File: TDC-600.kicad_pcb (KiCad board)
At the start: 2 copper layers, 99.9 x 64 mm, 32 parts, among them J1 MSXCART1, J2 Conn_01x03_Male, J3 Conn_01x03_Male, J4 Conn_01x03_Male, J5 Conn_01x03_Male, J6 FDD Connector, J7 ROM_SWITCH, SW1 SW_Push, U1 AT28C256, U2 74LS04, U3 74LS138, U4 WDC37C65, Y1 16Mhz

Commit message: Routing Release 1.0
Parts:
- J1: footprint Roni Footprints:MSX_CART_SW_Official_3Holes -> Roni_Footprints:MSX_CART_SW_Official
- moved R1 8.03 mm to (128.5, 48.5), turned to 180 degrees
- moved R11 2.84 mm to (122.7, 69.6)
- moved R9 0.48 mm to (82.4, 69.6)
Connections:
- J1 pad 41: Net-(J1-Pad41) -> GNDREF
- J1 pad 43: Net-(J1-Pad41) -> GNDREF
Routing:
- net GNDREF: track 0.00 -> 268.6 mm, vias 0 -> 5
- net +5V: track 0.00 -> 138.2 mm, vias 0 -> 1
- net /SLTSL: track 0.00 -> 125.7 mm, vias 0 -> 4
- net A14: track 0.00 -> 109.1 mm, vias 0 -> 4
- net /RESET: track 0.00 -> 106.1 mm, vias 0 -> 3
- net D7: track 0.00 -> 99.0 mm, vias 0 -> 2
- net A15: track 0.00 -> 96.6 mm, vias 0 -> 2
- net WDRST: track 0.00 -> 93.7 mm, vias 0 -> 2
- net A12: track 0.00 -> 92.0 mm, vias 0 -> 2
- net D6: track 0.00 -> 91.0 mm, vias 0 -> 1
- net /WR: track 0.00 -> 89.5 mm, vias 0 -> 3
- net A13: track 0.00 -> 87.0 mm
- net D5: track 0.00 -> 86.0 mm, vias 0 -> 2
- net A8: track 0.00 -> 81.8 mm, vias 0 -> 2
- net D4: track 0.00 -> 79.6 mm, vias 0 -> 1
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- added copper zone on B.Cu, net GNDREF
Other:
- outline, holes or cut-outs redrawn

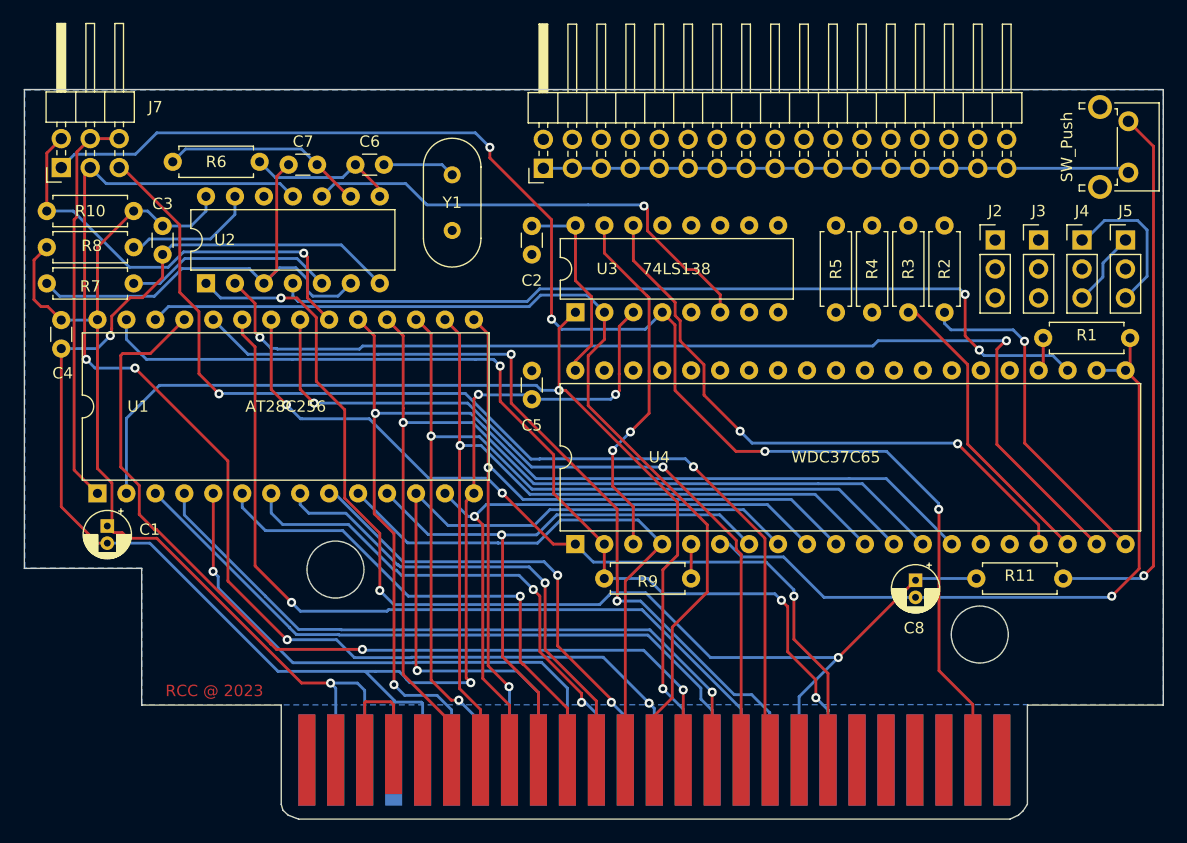
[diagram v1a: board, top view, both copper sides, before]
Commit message: Routing complete for Rev 1.0
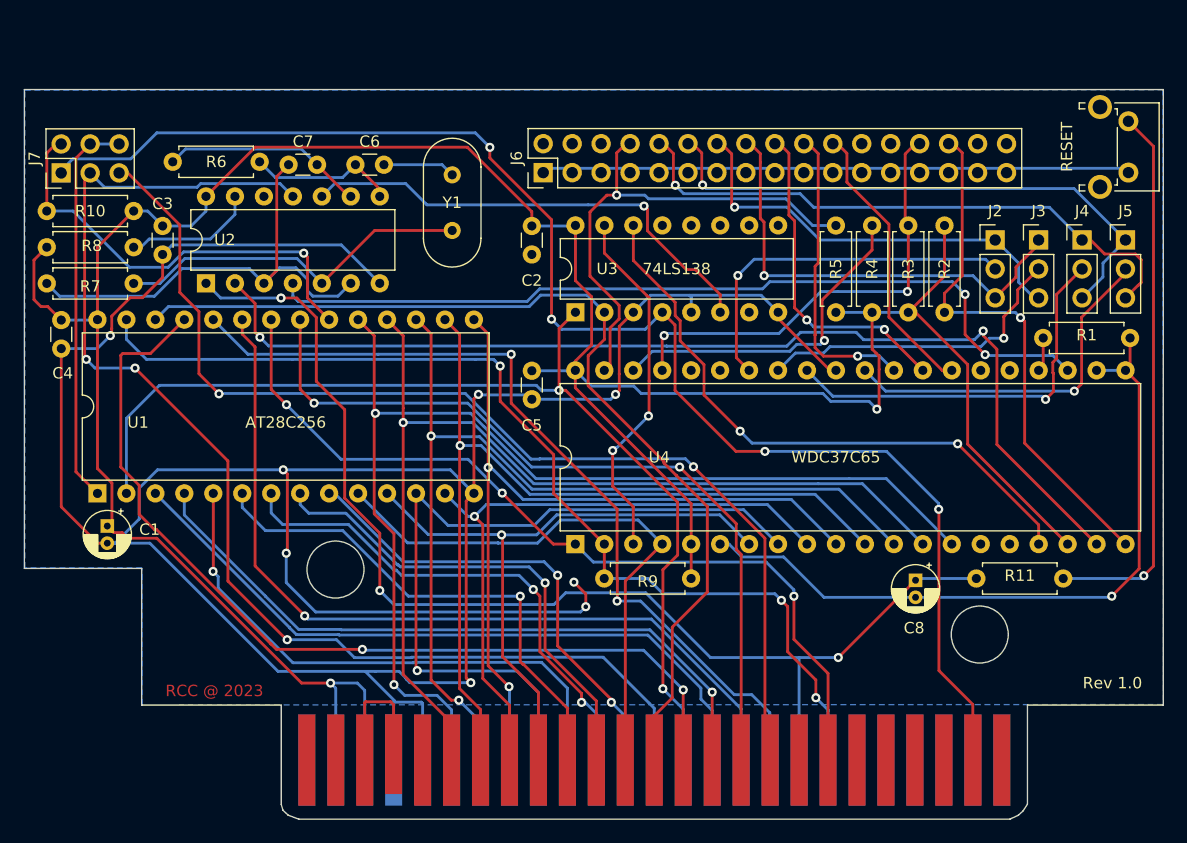
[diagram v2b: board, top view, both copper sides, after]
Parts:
- J6: footprint Connector_PinHeader_2.54mm:PinHeader_2x17_P2.54mm_Horizontal -> Connector_PinHeader_2.54mm:PinHeader_2x17_P2.54mm_Vertical
- J7: footprint Connector_PinHeader_2.54mm:PinHeader_2x03_P2.54mm_Horizontal -> Connector_PinHeader_2.54mm:PinHeader_2x03_P2.54mm_Vertical
- SW1: value SW_Push -> RESET
- moved J7 0.47 mm to (34.8, 34.0)
- moved J6 0.38 mm to (77.1, 34.0)
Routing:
- net +5V: track 138.2 -> 247.3 mm, vias 1 -> 2
- net GNDREF: track 268.6 -> 369.0 mm, vias 5 -> 9
- net INDEX: track 0.00 -> 44.2 mm, vias 0 -> 1
- net DS2: track 6.66 -> 50.3 mm, vias 0 -> 1
- net MOTORON2: track 0.00 -> 40.3 mm, vias 0 -> 1
- net WRITEPROTECT: track 0.00 -> 40.1 mm, vias 0 -> 2
- net DS1: track 13.5 -> 52.1 mm, vias 0 -> 1
- net MOTORON: track 0.00 -> 37.5 mm, vias 0 -> 1
- net /DS2: track 0.00 -> 34.8 mm, vias 0 -> 1
- net /MO2: track 0.00 -> 32.3 mm, vias 0 -> 1
- net /DS1: track 0.00 -> 31.7 mm, vias 0 -> 1
- net TRACK00: track 0.00 -> 30.1 mm, vias 0 -> 1
- net DIR: track 0.00 -> 29.1 mm, vias 0 -> 2
- net /MO1: track 0.00 -> 28.3 mm, vias 0 -> 1
- net STEP: track 0.00 -> 26.7 mm, vias 0 -> 1
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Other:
- board text added: "Rev 1.0"
